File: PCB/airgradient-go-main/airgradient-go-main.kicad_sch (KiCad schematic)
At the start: 203 parts, among them CN1 HCZZ0032-5, CN2 HCZZ0032-5, CN3 HCZZ0032-5, Q1 SIA445EDJ-T1-GE3, Q2 ZVN4106FTA_C508255, Q3 CSD83325L, Q4 SS8050-G, Q5 SI1308EDL, SW1 TS-1091C-A1B3-D2, SW2 TS-1091C-A1B3-D2, U1 W25N512GVEIG, U10 SGP41-D-R4, U11 PS1-CO-SMOKE-10k, U12 SHT4x, U13 SPL07-003, U14 LIS2DH12TR, U15 TMUX121NKGR_C22428404, U16 S12, U17 TCA6408ARGT, U18 TAU1113, U19 LM66200DRLR, U2 ZDSD512MLGEAG, U20 LP5036, U3 BQ27742YZFR-G1, U4 ESP32-C5-MINI-1, U5 BQ25628RYKR, U6 HYG-8503A, U7 TPL5010DDCR, U8 TPS63802DLAR, U9 TPS7A0228DQNR, Y1 32.768kHz CL6pF

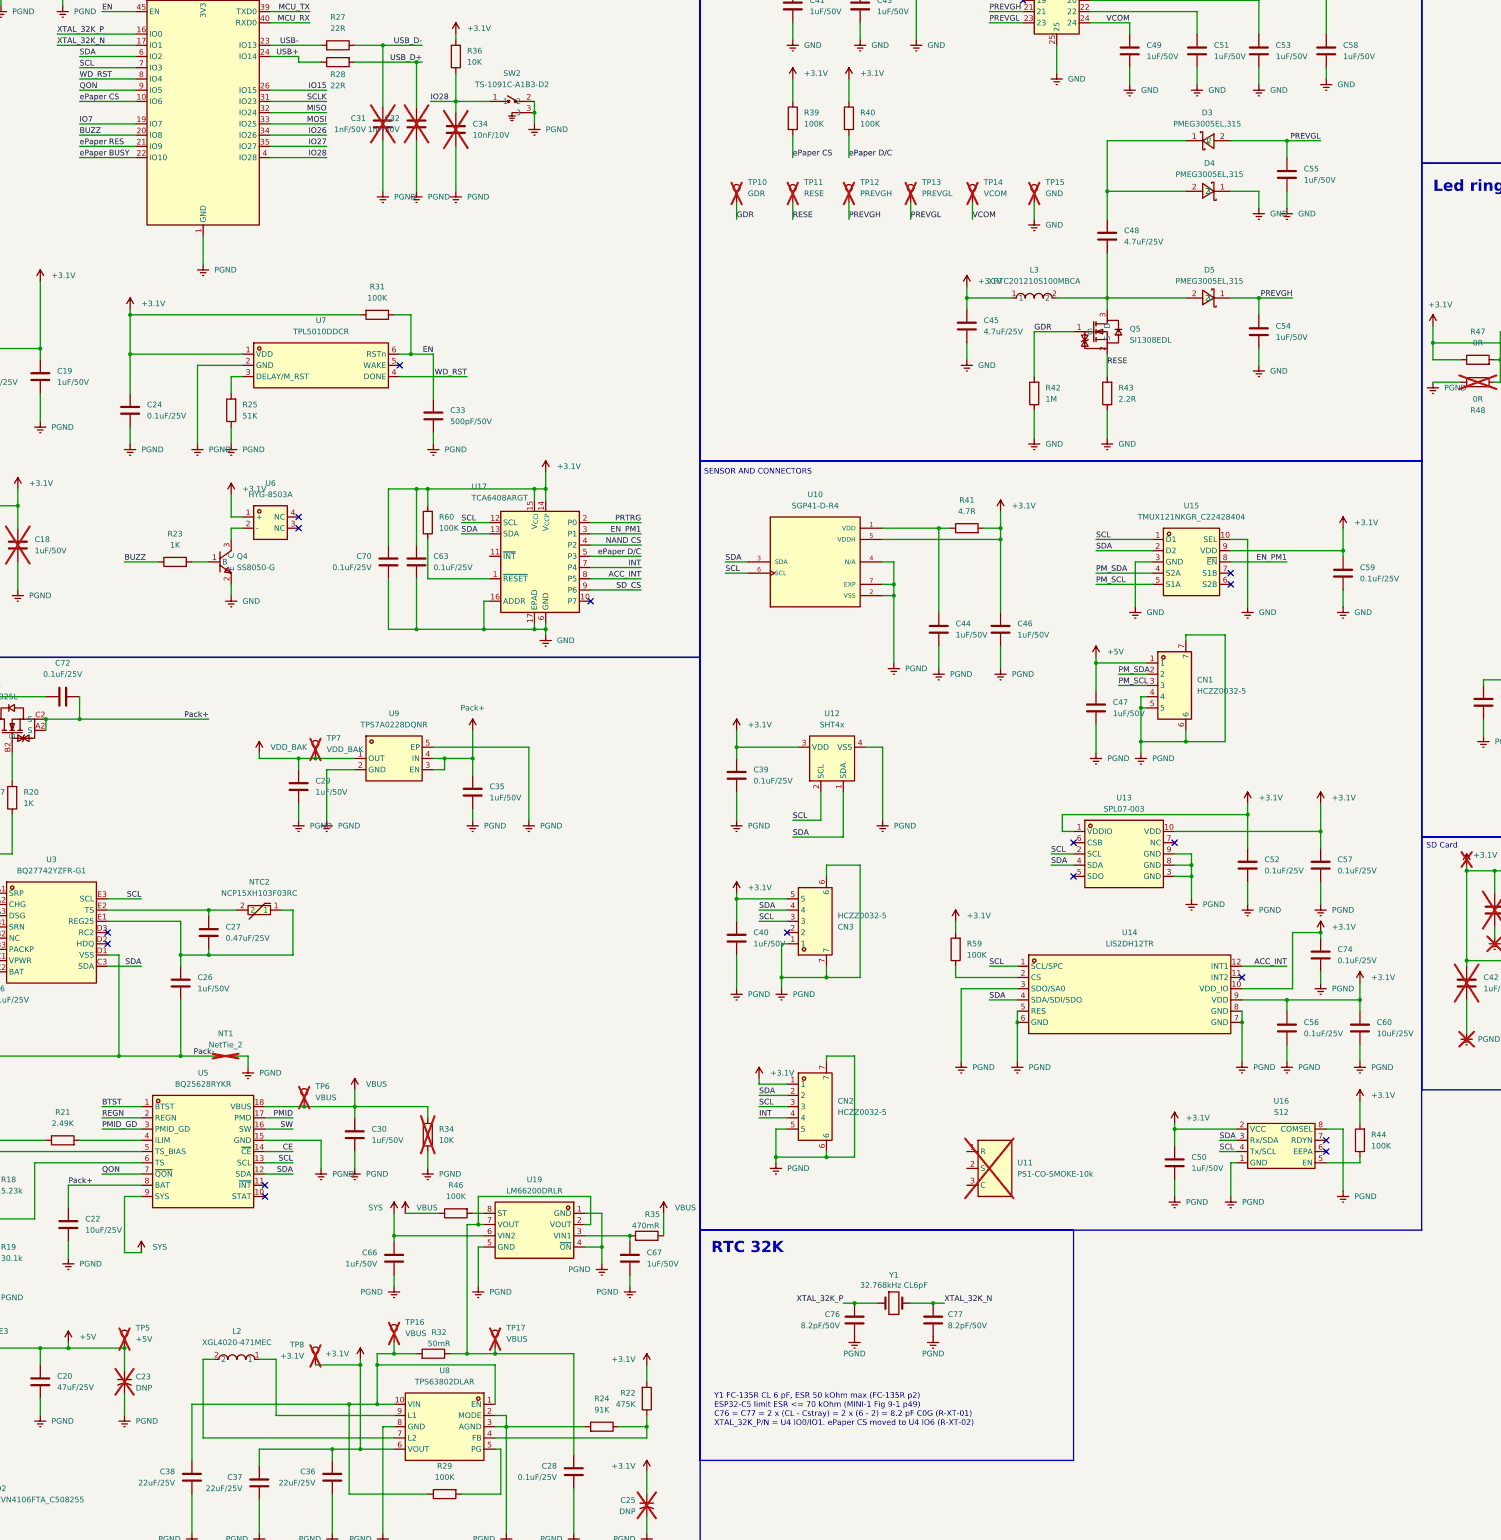
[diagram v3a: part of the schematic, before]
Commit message: Wire the charger and expander INT lines to IO15 and IO7
On v2.1 the BQ25628 ~INT (U5 pin 11) had an NC flag and the TCA6408A
~INT (U17 pin 11) floated, so charger events, touch (P4) and ACC_INT
(P5) could only be polled.

- CHG_INT: U5 ~INT -> U4 IO15 (pad 26). Direct, not via expander P7:
  INT is a 256 us low pulse (SLUSEG4C 8.3.8.3) and the TCA6408A clears
  its interrupt when the input returns (SCPS192E 8.3.3).
- EXP_INT: U17 ~INT -> U4 IO7 (pad 19). IO7 is the JTAG-source strap,
  ignored while EFUSE_JTAG_SEL_ENABLE = 0.
- New INT PULL-UPS block: R61/R62 10K to +3.1V (C327797, same as R26).
- Neither pin wakes deep sleep (GPIO0-6 only); R-INT-01..04.
- Hand edits: U4 labels IO7/IO15 renamed, U5/U17 INT labels drawn in
  the board's over-the-stub style, C63 field text moved below RESET.

lint: no new findings; ERC 269 -> 267; net_diff 0 errors.
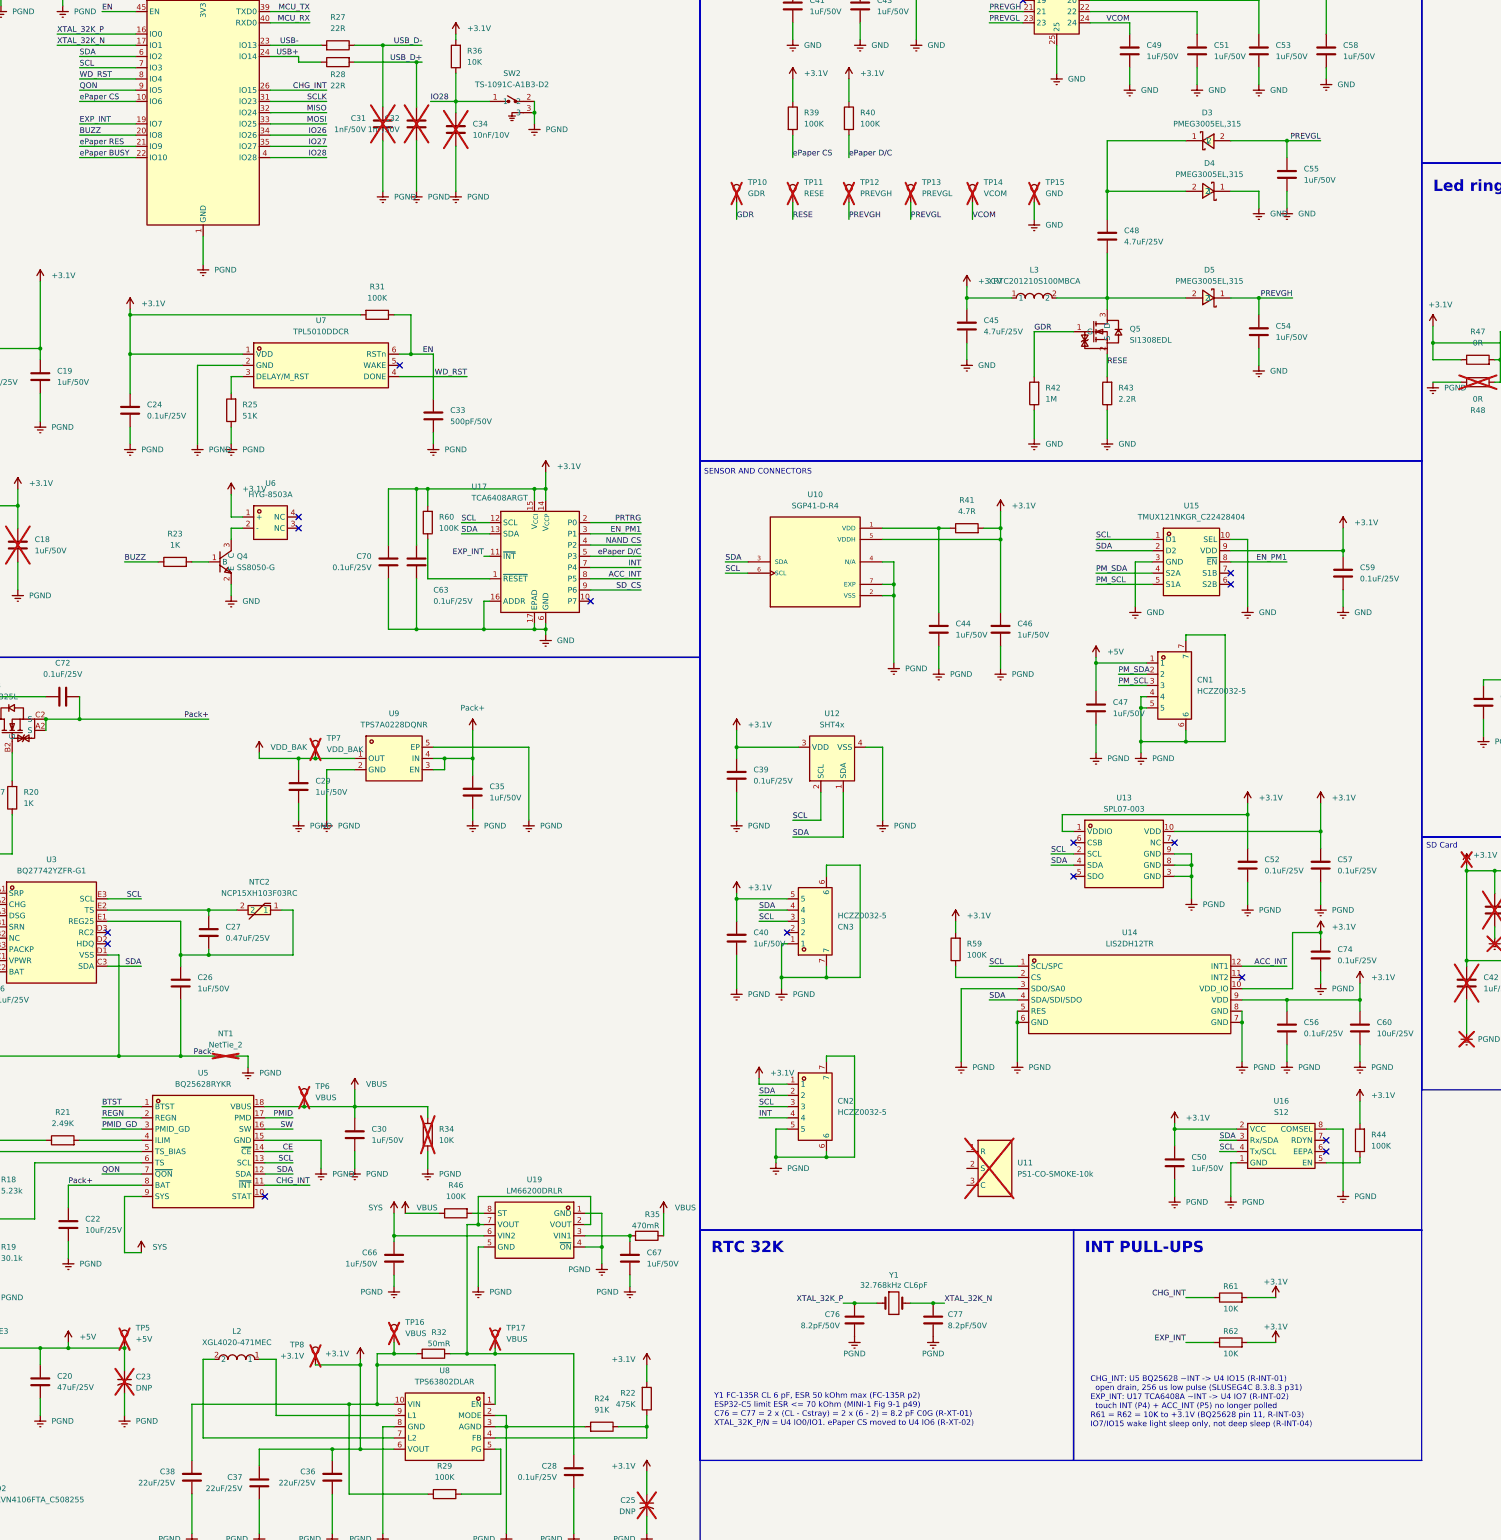
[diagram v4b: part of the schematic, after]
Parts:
- added R61, R62: 10K, Resistor_SMD:R_0402_1005Metric, symbol Device:R
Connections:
- net IO15 is gone; now on net CHG_INT: U4.26 (IO15)
- net IO7 is gone; now on net EXP_INT: U4.19 (IO7)
- net +3.1V: now also R61.2, R62.2
- net EXP_INT: now reaches U17.11 (~{INT})
- net EXP_INT: now also R62.1
- net CHG_INT: now reaches U5.11 (~{INT})
- net CHG_INT: now also R61.1
- no-connect marks 30 -> 29
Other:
- note added: "CHG_INT: U5 BQ25628 ~INT -> U4 IO15 (R-INT-01) open drain, 256 us low pulse (SLUSEG4C 8.3.8.3 p31) EXP_INT: U17 TCA6408A ~INT -> U4 IO7 (R-INT-02) touch INT (P4) + ACC_INT (P5) no longer polled R61 = R62 = 10K to +3.1V (BQ25628 pin 11, R-INT-03) IO7/IO15 wake light sleep only, not deep sleep (R-INT-04)"
- note added: "INT PULL-UPS"
